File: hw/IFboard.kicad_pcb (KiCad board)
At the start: 2 copper layers, 75 x 65.1 mm, 75 parts, among them J1 USB_C_Receptacle_USB2.0_16P, J2 Conn_01x03_Socket, J3 Conn_ARM_SWD_TagConnect_TC203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, J4 Conn_01x03_Socket, J5 Conn_01x03_Socket, J6 Conn_01x03_Socket, J7 Conn_01x01_MountingPin, SW3 SW_Push, SW4 SW_Push, SW5 SW_Push, SW6 SW_Push, U2 XC6206PxxxMR, U3 TCAN3413DR, U4 ST4E1240DT, U5 MAX232ESE+T, U6 STM32G0B1CBTx, U7 ER_OLEDM0.91_1x-I2C

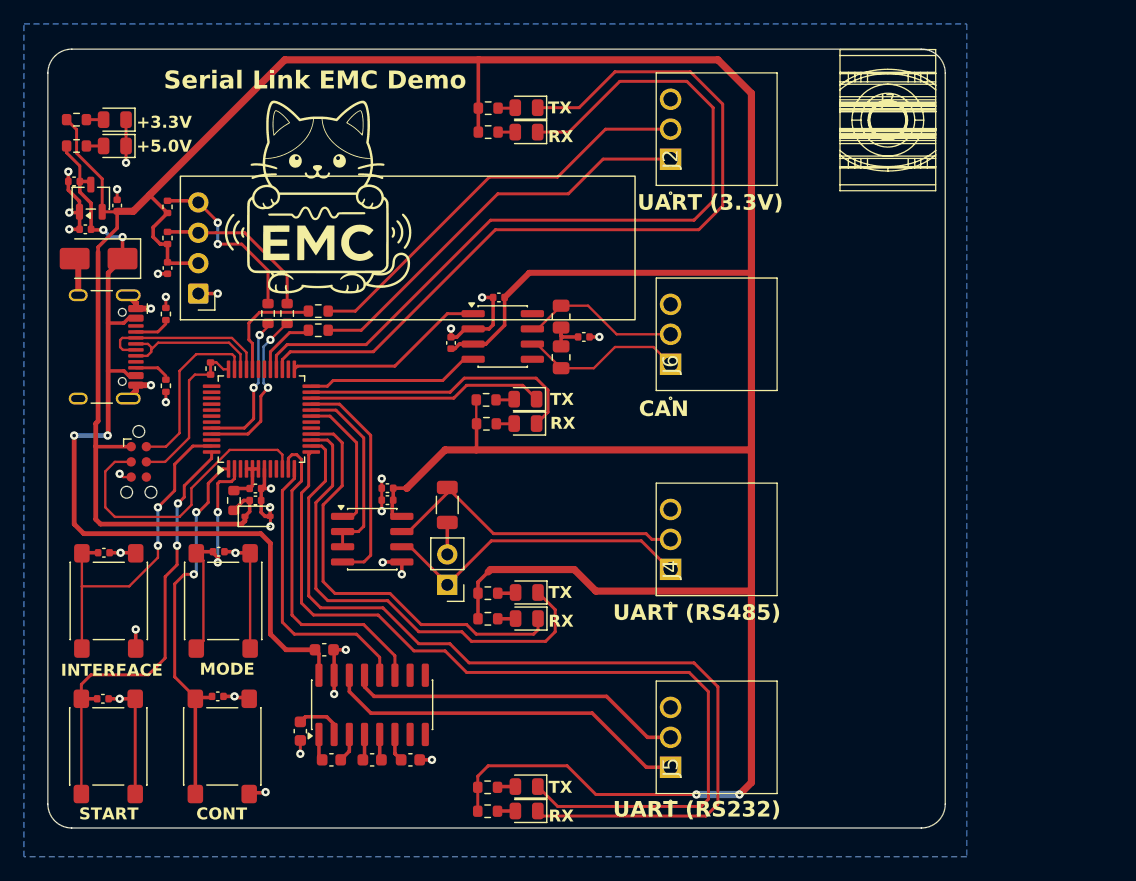
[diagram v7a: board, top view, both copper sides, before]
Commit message: added CMCs to RS485 and CAN interfaces
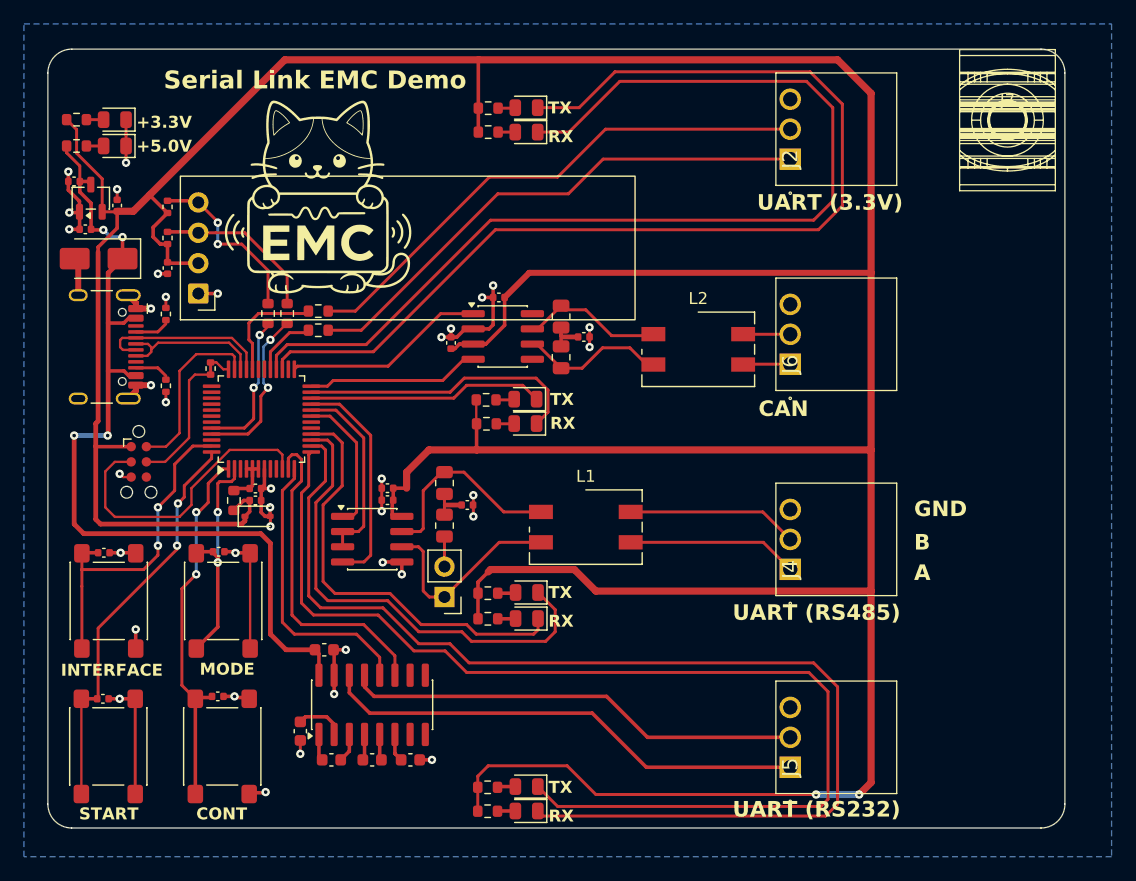
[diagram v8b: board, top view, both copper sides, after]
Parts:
- removed R6: 120, Resistor_SMD:R_1206_3216Metric
- added C24: 220p, Capacitor_SMD:C_0402_1005Metric, F.Cu at (86.0, 88.4)
- added L1: 1000 uH, PZL:L_Wurth_WE-SL2-74422x, F.Cu at (95.9, 90.3)
- added L2: 1000 uH, PZL:L_Wurth_WE-SL2-74422x, F.Cu at (105.3, 75.4)
- added R24: 56, Resistor_SMD:R_0805_2012Metric, F.Cu at (84.1, 90.2)
- added R25: 56, Resistor_SMD:R_0805_2012Metric, F.Cu at (84.1, 86.6)
- moved J7 10.0 mm to (131.1, 56.2)
- moved J2 10.0 mm to (113.0, 59.5)
- moved J4 10.0 mm to (113.0, 93.8)
- moved J5 10.0 mm to (113.0, 110.3)
- moved J6 10.0 mm to (113.0, 76.7)
- moved JP1 1.05 mm to (84.1, 96.1)
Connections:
- JP1 pad 1: Net-(J4-Pin_1) -> Net-(JP1-A)
- R14 pad 1: Net-(J6-Pin_2) -> Net-(U3-CANH)
- R15 pad 2: Net-(J6-Pin_1) -> Net-(U3-CANL)
- U3 pad 6: Net-(J6-Pin_1) -> Net-(U3-CANL)
- U3 pad 7: Net-(J6-Pin_2) -> Net-(U3-CANH)
- U4 pad 6: Net-(J4-Pin_1) -> Net-(JP1-A)
- U4 pad 7: Net-(J4-Pin_2) -> Net-(U4-B)
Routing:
- net +3.3V: track 312.0 -> 362.7 mm
- net /USART4_TX_LED: track 76.9 -> 96.9 mm
- net /USART4_RX_LED: track 74.2 -> 94.2 mm
- net /USART1_TX_LED: track 68.1 -> 88.1 mm
- net /USART1_RX_LED: track 69.3 -> 89.3 mm
- net Net-(JP1-A): track 0.00 -> 17.2 mm
- net Net-(U4-B): track 0.00 -> 16.9 mm
- net Net-(U3-CANL): track 0.00 -> 12.2 mm
- net Net-(J4-Pin_1): track 26.5 -> 14.3 mm
- net Net-(U3-CANH): track 0.00 -> 12.0 mm
- net Net-(J4-Pin_2): track 26.1 -> 14.3 mm
- net Net-(J2-Pin_2): track 34.9 -> 44.9 mm
- net Net-(J2-Pin_1): track 34.5 -> 44.5 mm
- net /USART4_RX_MAX: track 28.3 -> 38.3 mm
- net /USART4_TX_MAX: track 31.1 -> 40.9 mm
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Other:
- board size 75 x 65.1 mm -> 85 x 65.1 mm
- board text added: "A"
- board text added: "B"
- board text added: "GND"
